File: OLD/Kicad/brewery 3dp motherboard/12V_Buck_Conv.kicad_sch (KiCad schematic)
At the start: 31 parts, among them U10 DOZ45N03T, U5 LM25145RGYR, U9 DOZ45N03T

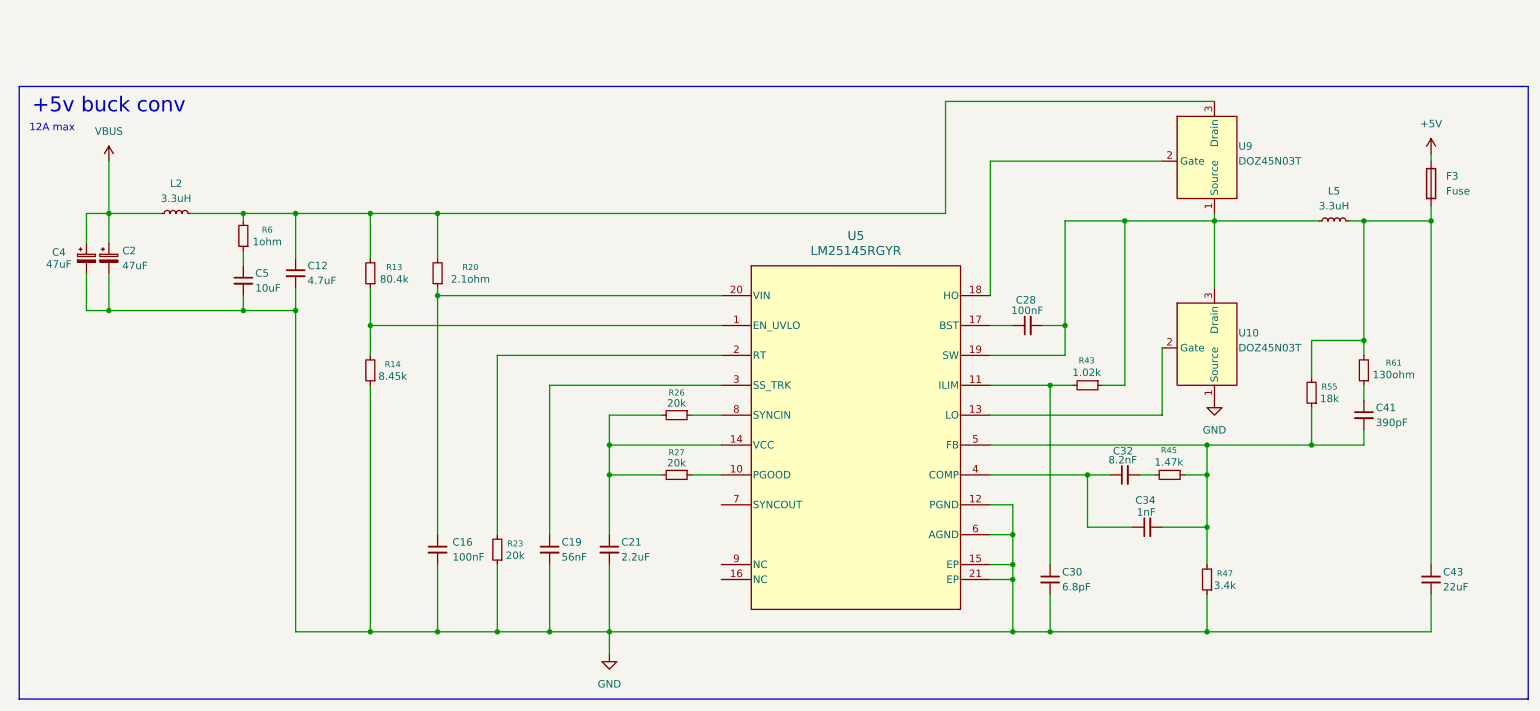
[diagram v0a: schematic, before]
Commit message: cleaned up structure a bit
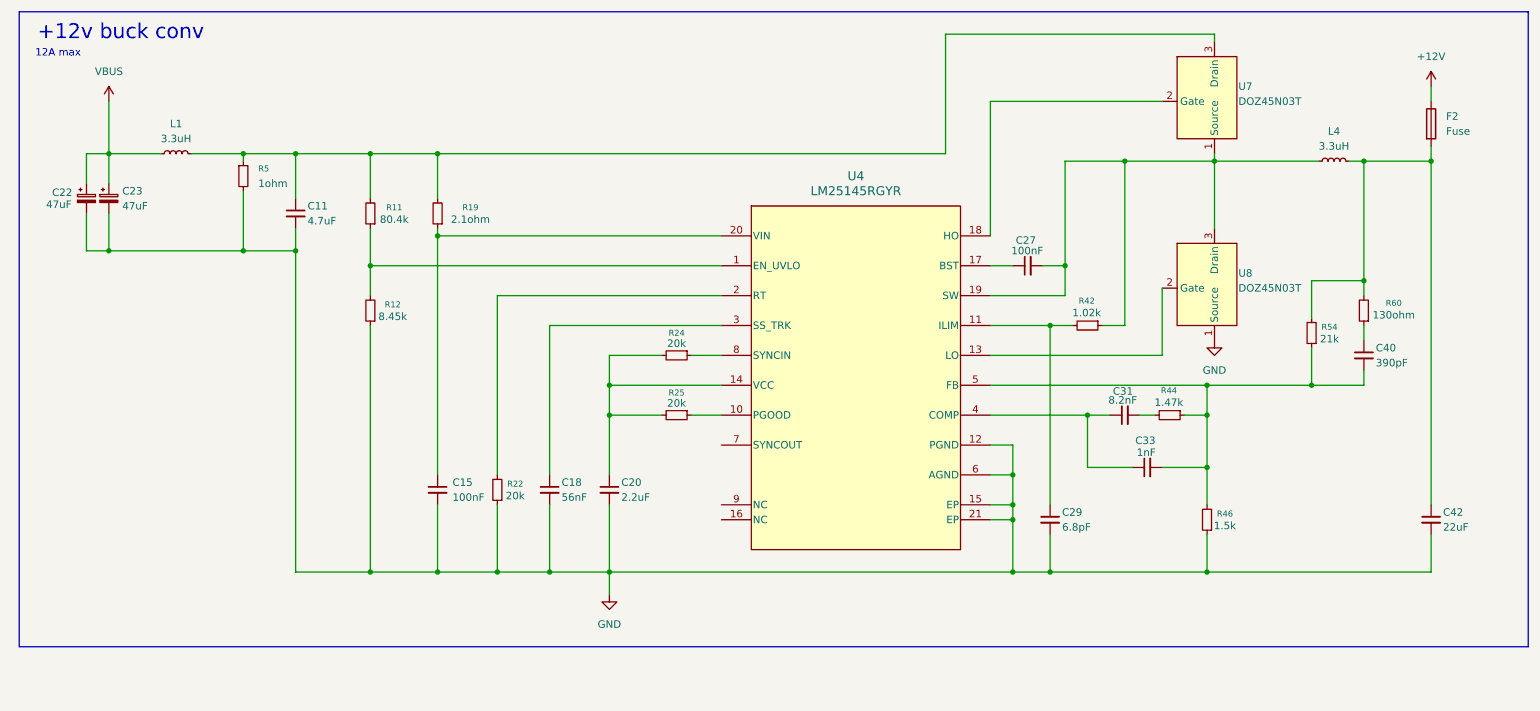
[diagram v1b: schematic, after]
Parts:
- removed C12: 4.7uF, Capacitor_SMD:C_1210_3225Metric, symbol Device:C_Small
- removed C16: 100nF, Capacitor_SMD:C_0402_1005Metric, symbol Device:C_Small
- removed C19: 56nF, Capacitor_SMD:C_0402_1005Metric, symbol Device:C_Small
- removed C2, C4: 47uF, Capacitor_THT:C_Radial_D6.3mm_H7.0mm_P2.50mm, symbol Device:C_Polarized_Small
- removed C21: 2.2uF, Capacitor_SMD:C_1206_3216Metric, symbol Device:C_Small
- removed C28: 100nF, Capacitor_SMD:C_0603_1608Metric, symbol Device:C_Small
- removed C30: 6.8pF, Capacitor_SMD:C_0402_1005Metric, symbol Device:C_Small
- removed C32: 8.2nF, Capacitor_SMD:C_0402_1005Metric, symbol Device:C_Small
- removed C34: 1nF, Capacitor_SMD:C_0402_1005Metric, symbol Device:C_Small
- removed C41: 390pF, Capacitor_SMD:C_0402_1005Metric, symbol Device:C_Small
- removed C43: 22uF, Capacitor_SMD:C_1210_3225Metric, symbol Device:C_Small
- removed C5: 10uF, Capacitor_SMD:C_1210_3225Metric, symbol Device:C_Small
- removed F3: Fuse, footprints:XF-509P, symbol Device:Fuse
- removed L2, L5: 3.3uH, footprints:IND_SRP1038A_BRN-M, symbol Device:L_Small
- removed R13: 80.4k, Resistor_SMD:R_0402_1005Metric, symbol Device:R_Small
- removed R14: 8.45k, Resistor_SMD:R_0402_1005Metric, symbol Device:R_Small
- removed R20: 2.1ohm, Resistor_SMD:R_0402_1005Metric, symbol Device:R_Small
- removed R23, R26, R27: 20k, Resistor_SMD:R_0402_1005Metric, symbol Device:R_Small
- removed R43: 1.02k, Resistor_SMD:R_0603_1608Metric, symbol Device:R_Small
- removed R45: 1.47k, Resistor_SMD:R_0402_1005Metric, symbol Device:R_Small
- removed R47: 3.4k, Resistor_SMD:R_0402_1005Metric, symbol Device:R_Small
- removed R55: 18k, Resistor_SMD:R_0402_1005Metric, symbol Device:R_Small
- removed R6: 1ohm, Resistor_SMD:R_0603_1608Metric, symbol Device:R_Small
- removed R61: 130ohm, Resistor_SMD:R_0402_1005Metric, symbol Device:R_Small
- removed U10, U9: DOZ45N03T, DOZ45N03T:DOZ45N03T, symbol DOZ45N03T:DOZ45N03T
- removed U5: LM25145RGYR, footprints:RGY0020B, symbol symbols:LM25145RGYR
- added C11: 4.7uF, Capacitor_SMD:C_0603_1608Metric, symbol Device:C_Small
- added C15, C27: 100nF, Capacitor_SMD:C_0402_1005Metric, symbol Device:C_Small
- added C18: 56nF, Capacitor_SMD:C_0402_1005Metric, symbol Device:C_Small
- added C20: 2.2uF, Capacitor_SMD:C_1206_3216Metric, symbol Device:C_Small
- added C22, C23: 47uF, Capacitor_THT:C_Radial_D6.3mm_H7.0mm_P2.50mm, symbol Device:C_Polarized_Small
- added C29: 6.8pF, Capacitor_SMD:C_0603_1608Metric, symbol Device:C_Small
- added C31: 8.2nF, Capacitor_SMD:C_0402_1005Metric, symbol Device:C_Small
- added C33: 1nF, Capacitor_SMD:C_0402_1005Metric, symbol Device:C_Small
- added C40: 390pF, Capacitor_SMD:C_0603_1608Metric, symbol Device:C_Small
- added C42: 22uF, Capacitor_SMD:C_1210_3225Metric, symbol Device:C_Small
- added F2: Fuse, footprints:XF-509P, symbol Device:Fuse
- added L1, L4: 3.3uH, footprints:IND_SRP1038A_BRN-M, symbol Device:L_Small
- added R11: 80.4k, Resistor_SMD:R_0402_1005Metric, symbol Device:R_Small
- added R12: 8.45k, Resistor_SMD:R_0402_1005Metric, symbol Device:R_Small
- added R19: 2.1ohm, Resistor_SMD:R_0402_1005Metric, symbol Device:R_Small
- added R22, R24, R25: 20k, Resistor_SMD:R_0402_1005Metric, symbol Device:R_Small
- added R42: 1.02k, Resistor_SMD:R_0402_1005Metric, symbol Device:R_Small
- added R44: 1.47k, Resistor_SMD:R_0402_1005Metric, symbol Device:R_Small
- added R46: 1.5k, Resistor_SMD:R_0402_1005Metric, symbol Device:R_Small
- added R5: 1ohm, Resistor_SMD:R_0603_1608Metric, symbol Device:R_Small
- added R54: 21k, Resistor_SMD:R_0402_1005Metric, symbol Device:R_Small
- added R60: 130ohm, Resistor_SMD:R_0402_1005Metric, symbol Device:R_Small
- added U4: LM25145RGYR, footprints:RGY0020B, symbol symbols:LM25145RGYR
- added U7, U8: DOZ45N03T, DOZ45N03T:DOZ45N03T, symbol DOZ45N03T:DOZ45N03T
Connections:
- net GND: now also C11.2, C15.2, C18.2, C20.2, C22.2, C23.2, C29.2, C42.2, R12.1, R22.1, R46.1, R5.2, U4.12 (PGND), U4.15 (EP), U4.21 (EP), U4.6 (AGND), U8.1 (Source)
- net VBUS: now also C22.1, C23.1, L1.1
- new net: C11.1, L1.2, R11.2, R19.2, R5.1, U7.3 (Drain)
- new net: U4.13 (LO), U8.2 (Gate)
- new net: C27.2, L4.1, R42.1, U4.19 (SW), U7.1 (Source), U8.3 (Drain)
- new net: C31.1, C33.1, U4.4 (COMP)
- new net: C31.2, R44.2
- new net: R24.1, U4.8 (SYNCIN)
- new net: C20.1, R24.2, R25.2, U4.14 (VCC)
- new net: C29.1, R42.2, U4.11 (ILIM)
- new net: C27.1, U4.17 (BST)
- new net: C33.2, C40.2, R44.1, R46.2, R54.1, U4.5 (FB)
- new net: C42.1, F2.2, L4.2, R54.2, R60.2
- new net: C40.1, R60.1
- new net: U4.18 (HO), U7.2 (Gate)
- new net: R22.2, U4.2 (RT)
- new net: R11.1, R12.2, U4.1 (EN_UVLO)
- new net: C15.1, R19.1, U4.20 (VIN)
- new net: C18.1, U4.3 (SS_TRK)
- new net: R25.1, U4.10 (PGOOD)
- new net +12V: F2.1
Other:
- note added: "+12v buck conv"
- note removed: "+5v buck conv"
